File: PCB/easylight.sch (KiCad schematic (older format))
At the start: 41 parts, among them J1 LiPo (1S/3.7V), J2 USB/PWR, J3 LEDs, J4 AVR-ISP, Q1 AO3415_C181094, SW0 SW_ON/OFF, SW1 SW_1, SW2 SW_2, SW3 SW_3, U1 ATtiny85-20PU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

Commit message: rename to easylight, add comments and TODOs
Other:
- note added: "TODO: rename"
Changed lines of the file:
@@
 encoding utf-8
 Sheet 1 1
-Title "Voronoi Box"
+Title "EasyLight"
 Date ""
 Rev ""
@@
 Text Notes 6250 5300 0    50   ~ 0
 TODO: Check pins
+Text Notes 7650 6950 0    50   ~ 0
+TODO: rename
 $EndSCHEMATC

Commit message: add (THT) part for attiny85, rename
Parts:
- U1: LCSC Part * -> C965497
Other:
- moved on the sheet: J4
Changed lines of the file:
@@
 F 2 "Package_DIP:DIP-8_W7.62mm" H 1750 4800 50  0001 C CIN
 F 3 "http://ww1.microchip.com/downloads/en/DeviceDoc/atmel-2586-avr-8-bit-microcontroller-attiny25-attiny45-attiny85_datasheet.pdf" H 1750 4800 50  0001 C CNN
-F 4 "*" H 1750 4800 50  0001 C CNN "LCSC Part"
+F 4 "C965497" H 1750 4800 50  0001 C CNN "LCSC Part"
 	1    1750 4800
 	1    0    0    -1
@@
 L Connector:AVR-ISP-6 J4
 U 1 1 63F240FE
-P 6000 4750
-F 0 "J4" H 5671 4846 50  0000 R CNN
-F 1 "AVR-ISP" H 5671 4755 50  0000 R CNN
-F 2 "Connector_PinHeader_2.54mm:PinHeader_2x03_P2.54mm_Vertical" V 5750 4800 50  0001 C CNN
-F 3 " ~" H 4725 4200 50  0001 C CNN
-	1    6000 4750
+P 5950 4900
+F 0 "J4" H 5621 4996 50  0000 R CNN
+F 1 "AVR-ISP" H 5621 4905 50  0000 R CNN
+F 2 "Connector_PinHeader_2.54mm:PinHeader_2x03_P2.54mm_Vertical" V 5700 4950 50  0001 C CNN
+F 3 " ~" H 4675 4350 50  0001 C CNN
+	1    5950 4900
 	1    0    0    -1
 $EndComp
@@
 L power:GND #PWR0109
 U 1 1 63F26206
-P 5900 5150
-F 0 "#PWR0109" H 5900 4900 50  0001 C CNN
-F 1 "GND" H 5905 4977 50  0000 C CNN
-F 2 "" H 5900 5150 50  0001 C CNN
-F 3 "" H 5900 5150 50  0001 C CNN
-	1    5900 5150
+P 5850 5300
+F 0 "#PWR0109" H 5850 5050 50  0001 C CNN
+F 1 "GND" H 5855 5127 50  0000 C CNN
+F 2 "" H 5850 5300 50  0001 C CNN
+F 3 "" H 5850 5300 50  0001 C CNN
+	1    5850 5300
 	1    0    0    -1
 $EndComp
@@
 L power:VCC #PWR0110
 U 1 1 63F267A8
-P 5900 4250
-F 0 "#PWR0110" H 5900 4100 50  0001 C CNN
-F 1 "VCC" H 5915 4423 50  0000 C CNN
-F 2 "" H 5900 4250 50  0001 C CNN
-F 3 "" H 5900 4250 50  0001 C CNN
-	1    5900 4250
-	1    0    0    -1
-$EndComp
-Text Notes 5000 3950 0    50   ~ 0
+P 5850 4400
+F 0 "#PWR0110" H 5850 4250 50  0001 C CNN
+F 1 "VCC" H 5865 4573 50  0000 C CNN
+F 2 "" H 5850 4400 50  0001 C CNN
+F 3 "" H 5850 4400 50  0001 C CNN
+	1    5850 4400
+	1    0    0    -1
+$EndComp
+Text Notes 4950 4100 0    50   ~ 0
 Turn off and disconnect LEDs while programming
-Text Label 6400 4850 0    50   ~ 0
+Text Label 6350 5000 0    50   ~ 0
 RESET
-Text Label 6400 4650 0    50   ~ 0
+Text Label 6350 4800 0    50   ~ 0
 AREF
-Text Label 6400 4750 0    50   ~ 0
+Text Label 6350 4900 0    50   ~ 0
 D_LEDS2
-Text Label 6400 4550 0    50   ~ 0
+Text Label 6350 4700 0    50   ~ 0
 D_LEDS
 Wire Wire Line
@@
 Wire Wire Line
 	2600 1450 2600 1250
-Text Notes 6250 5300 0    50   ~ 0
+Text Notes 6200 5450 0    50   ~ 0
 TODO: Check pins
 Text Notes 7650 6950 0    50   ~ 0

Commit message: add TVS for ESD protection, another P-FET for reverse polarity protection
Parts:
- removed D1: SS34_C8678, lcsc:SMA_L4.3-W2.6-LS5.2-RD, symbol LCSC:SS34_C8678
- added D1: P6SMB6.8CA-C78395, lcsc:SMB_L4.6-W3.6-LS5.3-BI, symbol LCSC:P6SMB6.8CA-C78395
- added H3: MountingHole, MountingHole:MountingHole_3.2mm_M3_Pad, symbol Mechanical:MountingHole
- added Q2: AO3415_C181094, lcsc:SOT-23-3_L2.9-W1.3-P1.90-LS2.4-BR, symbol LCSC:AO3415_C181094
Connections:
- net GND: now also D1.2, Q2.1 (G)
- net VBUS: now also Q2.2 (S); no longer F1.1
- new net: D1.1, F1.1, Q2.3 (D)
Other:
- note added: "Reverse polarity protection: Q2 \nShort circuit protection: F1\nESD: D1"
- note removed: "Reverse polarity should be short-circuited through diode, \nwhich triggers short circuit protection F1."
- moved on the sheet: C1, C3, C7, F1, H1, H2, JP1, R2, R4, TP3, U2

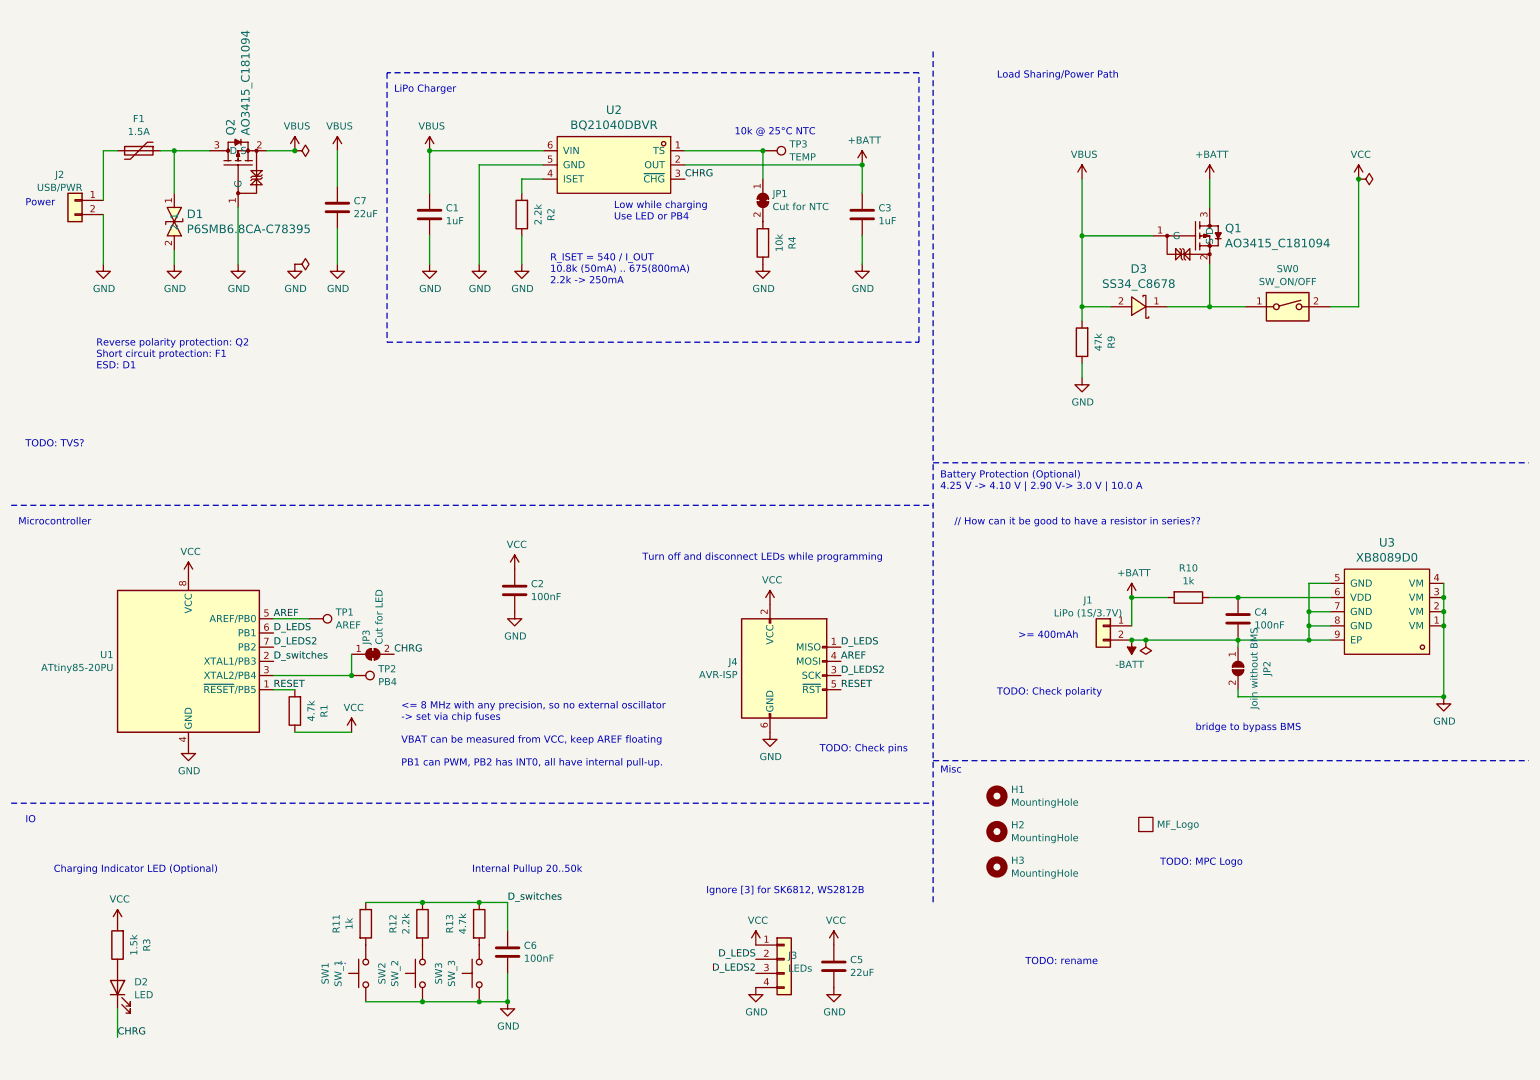
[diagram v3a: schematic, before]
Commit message: layout PCB, add series resistors for LEDs, remove unused components and add some cosmetics; ratsnest WIP
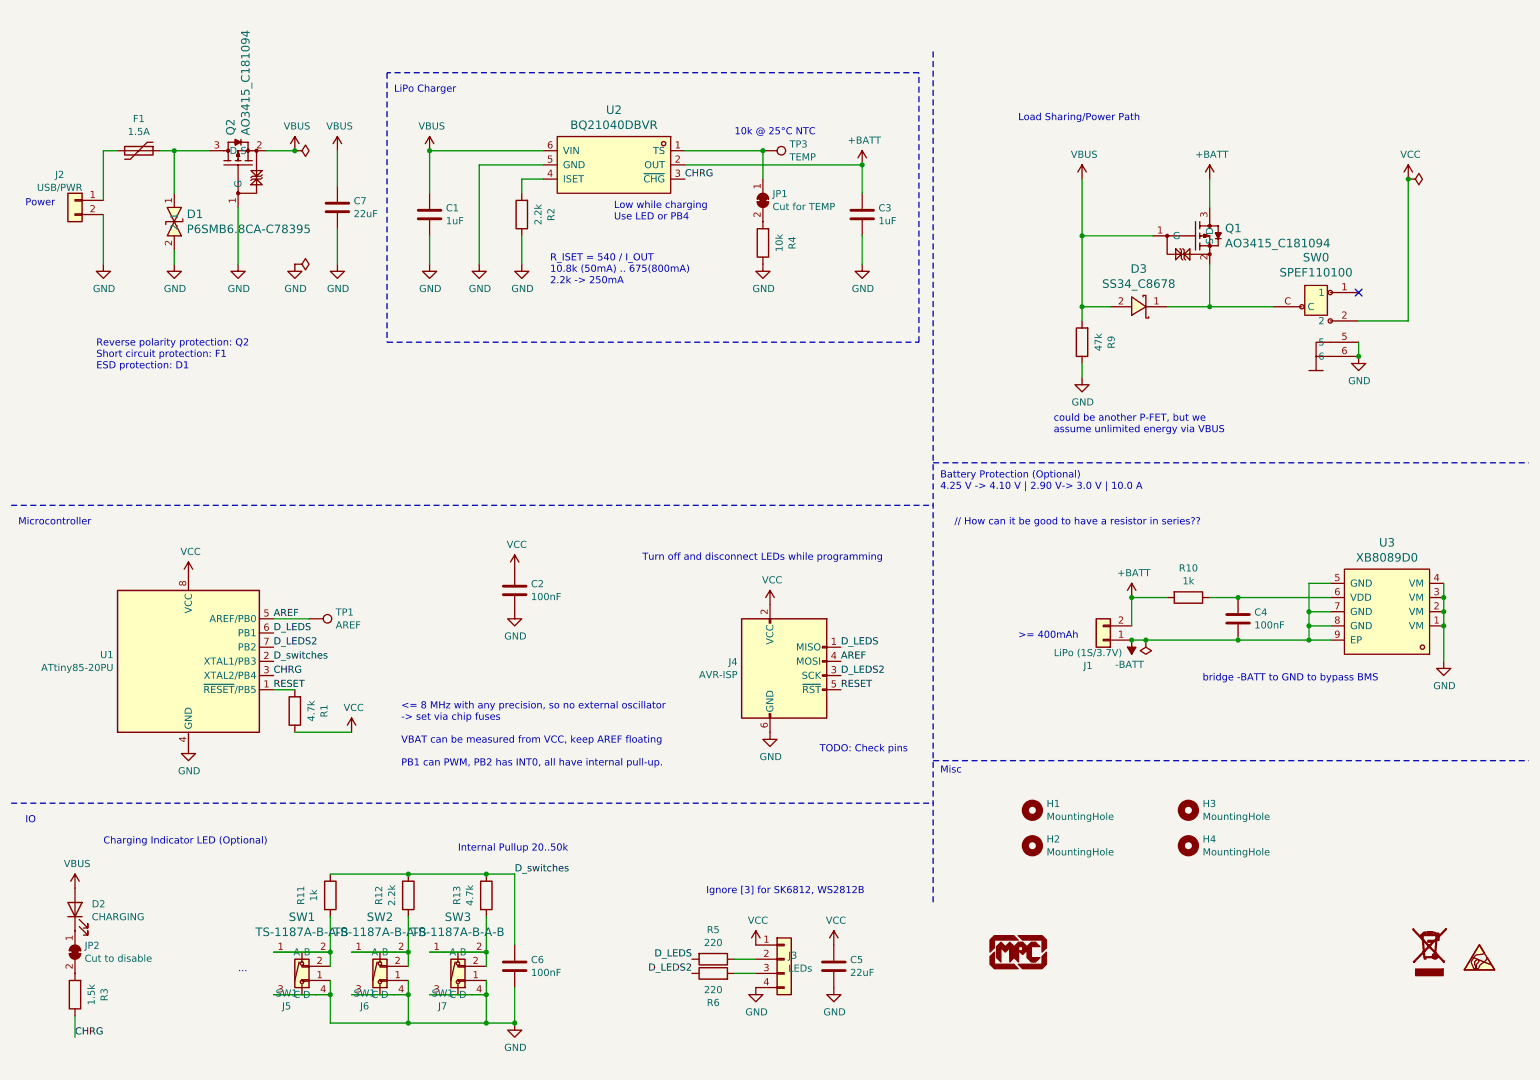
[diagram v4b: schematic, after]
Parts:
- removed JP2: Join without BMS, Jumper:SolderJumper-2_P1.3mm_Open_RoundedPad1.0x1.5mm, symbol Jumper:SolderJumper_2_Open
- removed JP3: Cut for LED, Jumper:SolderJumper-2_P1.3mm_Bridged_RoundedPad1.0x1.5mm, symbol Jumper:SolderJumper_2_Bridged
- removed L1: MF_Logo, MF custom:mf_logo_10mm, symbol MF_custom:MF_Logo
- removed SW0: SW_ON/OFF, symbol Switch:SW_DIP_x01
- removed SW1: SW_1, Button_Switch_THT:SW_PUSH_6mm_H4.3mm, symbol Switch:SW_Push
- removed SW2: SW_2, Button_Switch_THT:SW_PUSH_6mm_H4.3mm, symbol Switch:SW_Push
- removed SW3: SW_3, Button_Switch_THT:SW_PUSH_6mm_H4.3mm, symbol Switch:SW_Push
- removed TP2: PB4, TestPoint:TestPoint_THTPad_D2.0mm_Drill1.0mm, symbol Connector:TestPoint
- added G1: LOGO, Symbol:WEEE-Logo_4.2x6mm_SilkScreen, symbol WEEEE:LOGO
- added H4: MountingHole, MountingHole:MountingHole_3.2mm_M3_Pad, symbol Mechanical:MountingHole
- added J5, J6, J7: SW1, Connector_PinHeader_2.54mm:PinHeader_1x02_P2.54mm_Vertical, symbol Connector_Generic:Conn_01x02
- added JP2: Cut to disable, Jumper:SolderJumper-2_P1.3mm_Bridged_RoundedPad1.0x1.5mm, symbol Jumper:SolderJumper_2_Bridged
- added L1: LOGO, MF custom:mpc_logo_10mm, symbol MPC:LOGO
- added R5, R6: 220, Resistor_SMD:R_0603_1608Metric_Pad1.05x0.95mm_HandSolder, symbol Device:R
- added SW0: SPEF110100, lcsc:SW-TH_SPEF110100, symbol LCSC:SPEF110100
- added SW1, SW2, SW3: TS-1187A-B-A-B, lcsc:SW-SMD_4P-L5.1-W5.1-P3.70-LS6.5-TL-2, symbol LCSC:TS-1187A-B-A-B
- added SYM1: SYM_ESD_Small, Symbol:ESD-Logo_6.6x6mm_SilkScreen, symbol Graphic:SYM_ESD_Small
- D2: value LED -> CHARGING
- JP1: value Cut for NTC -> Cut for TEMP
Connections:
- net +BATT: now also J1.2 (Pin_2); no longer J1.1 (Pin_1)
- net -BATT: now also J1.1 (Pin_1); no longer J1.2 (Pin_2)
- net CHRG: now also R3.1, U1.3 (XTAL2/PB4); no longer D2.1 (K)
- net D_LEDS: now also R5.2; no longer J3.2 (Pin_2)
- net D_LEDS2: now also R6.1; no longer J3.3 (Pin_3)
- net GND: now also J5.1 (Pin_1), J6.1 (Pin_1), J7.1 (Pin_1), SW0.5, SW0.6, SW1.3 (C), SW1.4 (D), SW2.3 (C), SW2.4 (D), SW3.3 (C), SW3.4 (D)
- net VBUS: now also D2.2 (A)
- net VCC: now also SW0.2; no longer R3.2
- net at D3.1, Q1.2 (S): now also SW0.C
- net at R11.2: now also J5.2 (Pin_2), SW1.1 (A), SW1.2 (B)
- net at R13.2: now also J7.2 (Pin_2), SW3.1 (A), SW3.2 (B)
- net at R12.2: now also J6.2 (Pin_2), SW2.1 (A), SW2.2 (B)
- new net: D2.1 (K), JP2.1 (A)
- new net: JP2.2 (B), R3.2
- new net: J3.2 (Pin_2), R5.1
- new net: J3.3 (Pin_3), R6.2
- no-connect marks 0 -> 1
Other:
- note added: "Reverse polarity protection: Q2 \nShort circuit protection: F1\nESD protection: D1"
- note added: "bridge -BATT to GND to bypass BMS"
- note added: "could be another P-FET, but we \nassume unlimited energy via VBUS"
- note removed: "Reverse polarity protection: Q2 \nShort circuit protection: F1\nESD: D1"
- note removed: "TODO: Check polarity"
- note removed: "TODO: MPC Logo"
- note removed: "TODO: TVS?"
- note removed: "TODO: rename"
- note removed: "bridge to bypass BMS"
- moved on the sheet: C6, D2, H1, H2, H3, R11, R12, R13, R3

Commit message: minor cleanup
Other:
- note removed: "// How can it be good to have a resistor in series??"
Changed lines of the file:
@@
 F 1 "XB8089D0" H 10200 4069 60  0000 C CNN
 F 2 "lcsc:SOIC-8_L4.9-W3.9-P1.27-LS6.0-BL-EP3.3-1" H 10200 3950 60  0001 C CNN
-F 3 "" H 10200 4450 50  0001 C CNN
+F 3 "https://www.lcsc.com/product-detail/Battery-Management-ICs_XySemi-XB8089D0_C2760005.html" H 10200 4450 50  0001 C CNN
 F 4 "xysemi(赛芯微)" H 10200 4450 0   0001 C CNN "Manufacturer"
 F 5 "C2760005" H 10200 4450 0   0001 C CNN "LCSC Part"
@@
 Text Notes 7050 3600 0    50   ~ 0
 Battery Protection (Optional)\n4.25 V -> 4.10 V | 2.90 V-> 3.0 V | 10.0 A
-Text Notes 7150 3850 0    50   ~ 0
-// How can it be good to have a resistor in series??
 Text Notes 8900 4950 0    50   ~ 0
 bridge -BATT to GND to bypass BMS

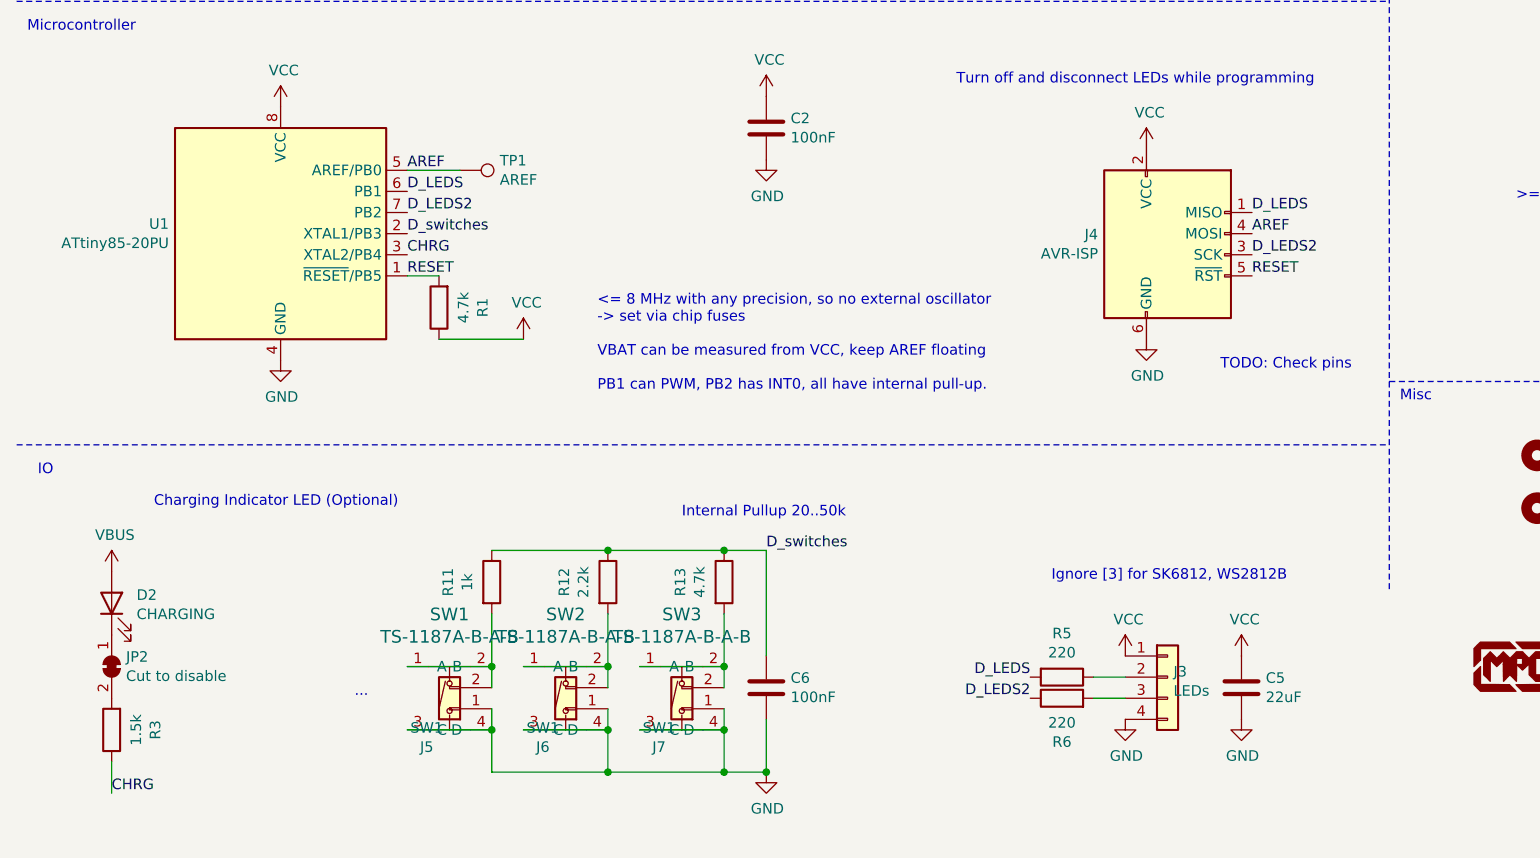
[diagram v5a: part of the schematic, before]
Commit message: add dedicated pullup for resistor ladder, add docs, finish routing of PCB
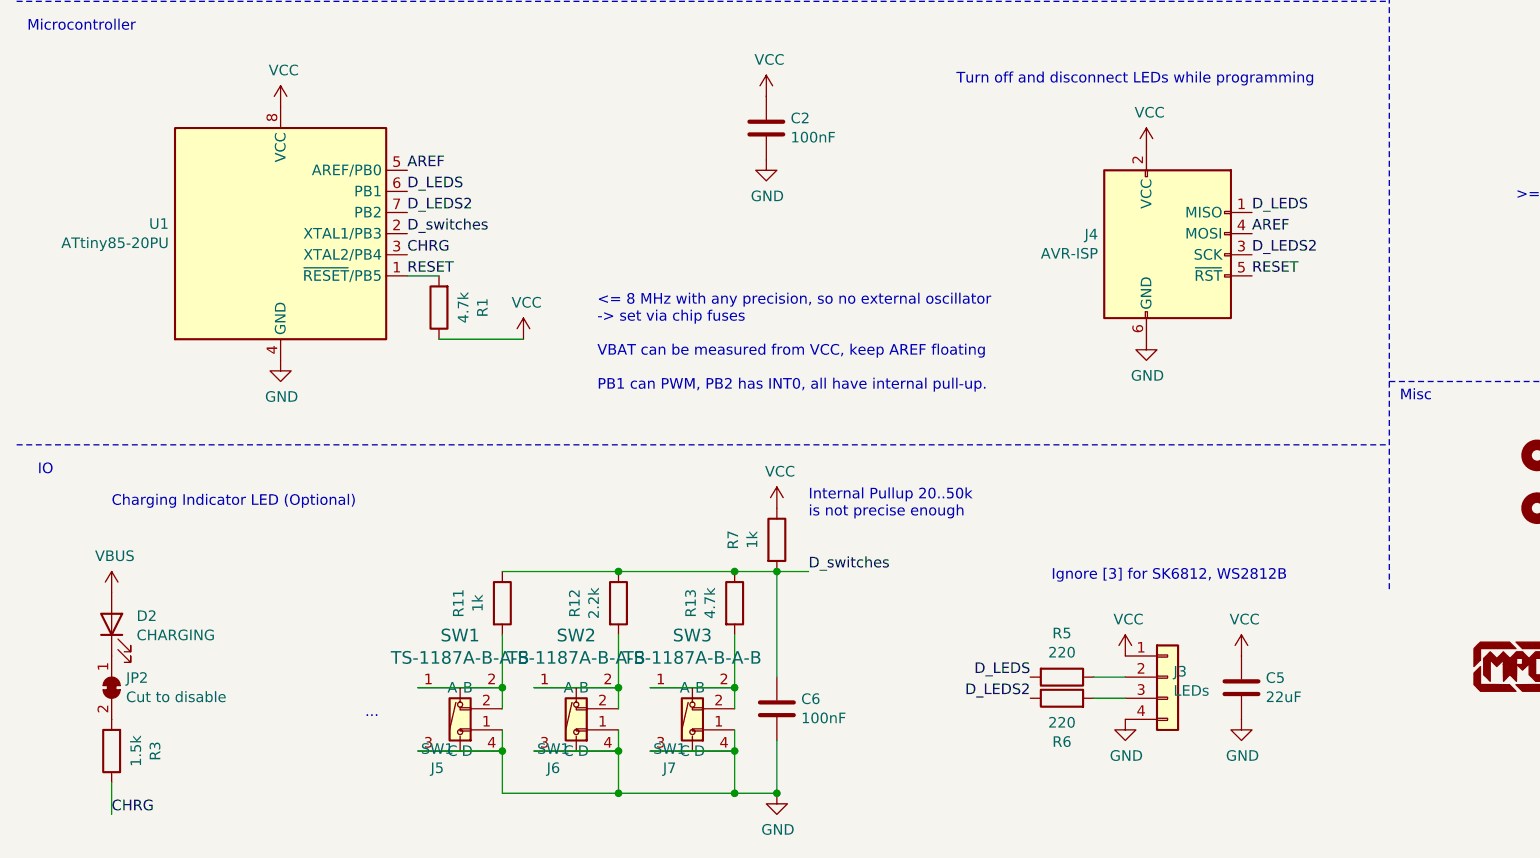
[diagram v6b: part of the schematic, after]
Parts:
- removed TP1: AREF, TestPoint:TestPoint_Pad_D1.5mm, symbol Connector:TestPoint
- added R7: 1k, Resistor_SMD:R_0603_1608Metric_Pad1.05x0.95mm_HandSolder, symbol Device:R
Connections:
- net D_switches: now also R7.2
- net VCC: now also R7.1
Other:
- note added: "Internal Pullup 20..50k \nis not precise enough"
- note removed: "Internal Pullup 20..50k"
- note removed: "TODO: Check pins"
- moved on the sheet: C6, D2, J5, J6, J7, JP2, R11, R12, R13, R3, SW1, SW2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
